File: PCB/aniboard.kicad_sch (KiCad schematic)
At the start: 416 parts, among them J2 Conn_01x02_Pin, J3 Conn_01x02_Pin, J5 Conn_01x03_Pin, J6 USB_C_Receptacle_USB2.0_14P, J7 USB_C_Receptacle_USB2.0_14P, SW1 SW_Push, SW10 SW_Push, SW11 SW_Push, SW12 SW_Push, SW13 SW_Push, SW14 SW_Push, SW15 SW_Push, SW16 SW_Push, SW17 SW_Push, SW18 SW_Push, SW19 SW_Push, SW2 SW_Push, SW20 SW_Push, SW21 SW_Push, SW22 SW_Push, SW23 SW_Push, SW24 SW_Push, SW25 SW_Push, SW26 SW_Push, SW27 SW_Push, SW28 SW_Push, SW29 SW_Push, SW3 SW_Push, SW30 SW_Push, SW31 SW_Push, SW32 SW_Push, SW33 SW_Push, SW34 SW_Push, SW35 SW_Push, SW36 SW_Push, SW37 SW_Push, SW38 SW_Push, SW39 SW_Push, SW4 SW_Push, SW40 SW_Push, SW41 SW_Push, SW42 SW_Push, SW43 SW_Push, SW44 SW_Push, SW45 SW_Push, SW46 SW_Push, SW47 SW_Push, SW48 SW_Push, SW49 SW_Push, SW5 SW_Push, SW50 SW_Push, SW51 SW_Push, SW52 SW_Push, SW53 SW_Push, SW54 SW_Push, SW55 SW_Push, SW56 SW_Push, SW57 SW_Push, SW58 SW_Push, SW59 SW_Push, SW6 SW_Push, SW60 SW_Push, SW61 SW_Push, SW62 SW_Push, SW63 SW_Push, SW64 SW_Push, SW65 SW_Push, SW66 SW_Push, SW67 SW_Push, SW68 SW_Push, SW69 SW_Push, SW7 SW_Push, SW70 SW_Push, SW71 SW_Push, SW72 SW_Push, SW73 SW_Push, SW74 SW_Push, SW75 SW_Push, SW76 SW_Push, SW77 SW_Push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

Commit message: V4
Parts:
- added D95: LED, LED_SMD:LED_0603_1608Metric_Pad1.05x0.95mm_HandSolder, symbol Device:LED
- added R20: 200Ω, Resistor_SMD:R_0805_2012Metric_Pad1.20x1.40mm_HandSolder, symbol Device:R
- added U7: ESP-12E, RF_Module:ESP-12E, symbol RF_Module:ESP-12E
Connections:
- net +3.3V: now also U7.1 (~{RST}), U7.3 (EN), U7.8 (VCC)
- net GND: now also R20.1, U7.15 (GND)
- net SCL: now reaches Brd1.3 (SCL), R10.2, U4.7 (GPIO5)
- net SCL: now also U7.5 (GPIO14)
- net SDA: now reaches Brd1.4 (SDA), R11.2, U4.6 (GPIO4)
- net SDA: now also U7.17 (GPIO2)
- new net: D95.2 (A), U7.7 (GPIO13)
- new net: D95.1 (K), R20.2
- no-connect marks 5 -> 20
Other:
- note added: "Bluetooth module"

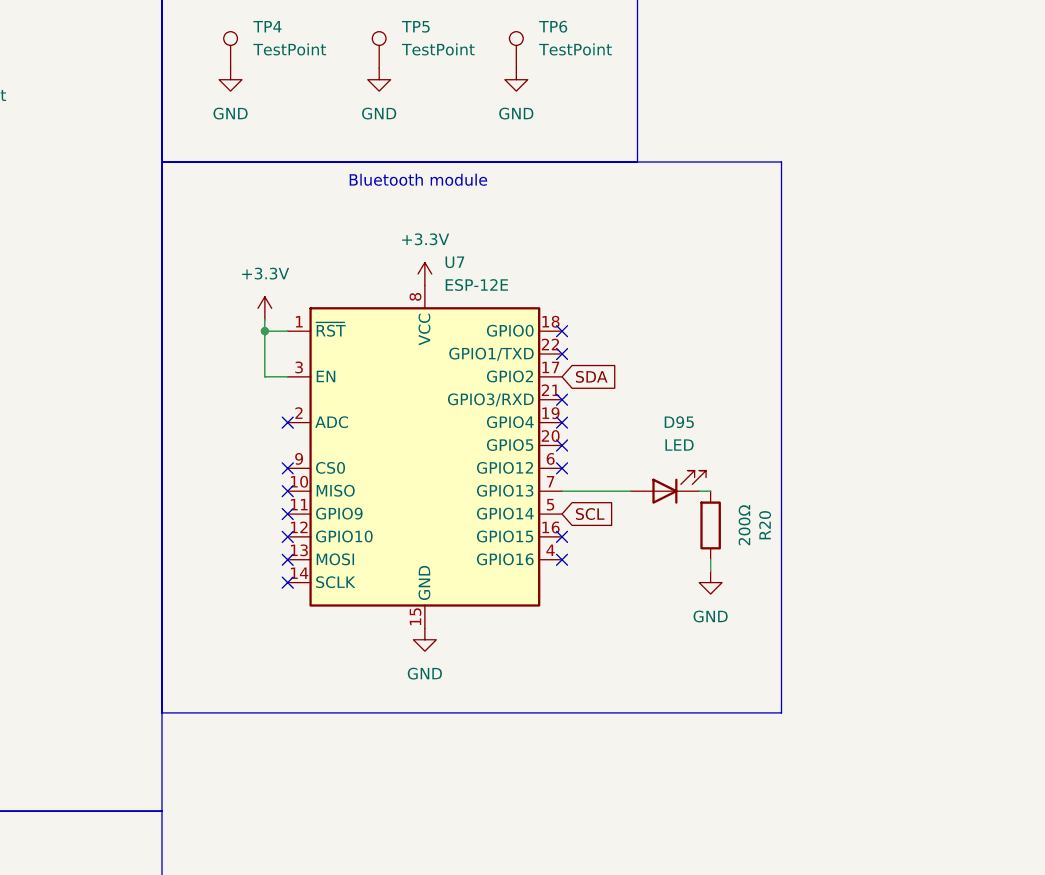
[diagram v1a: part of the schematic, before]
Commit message: RX TX Breakout
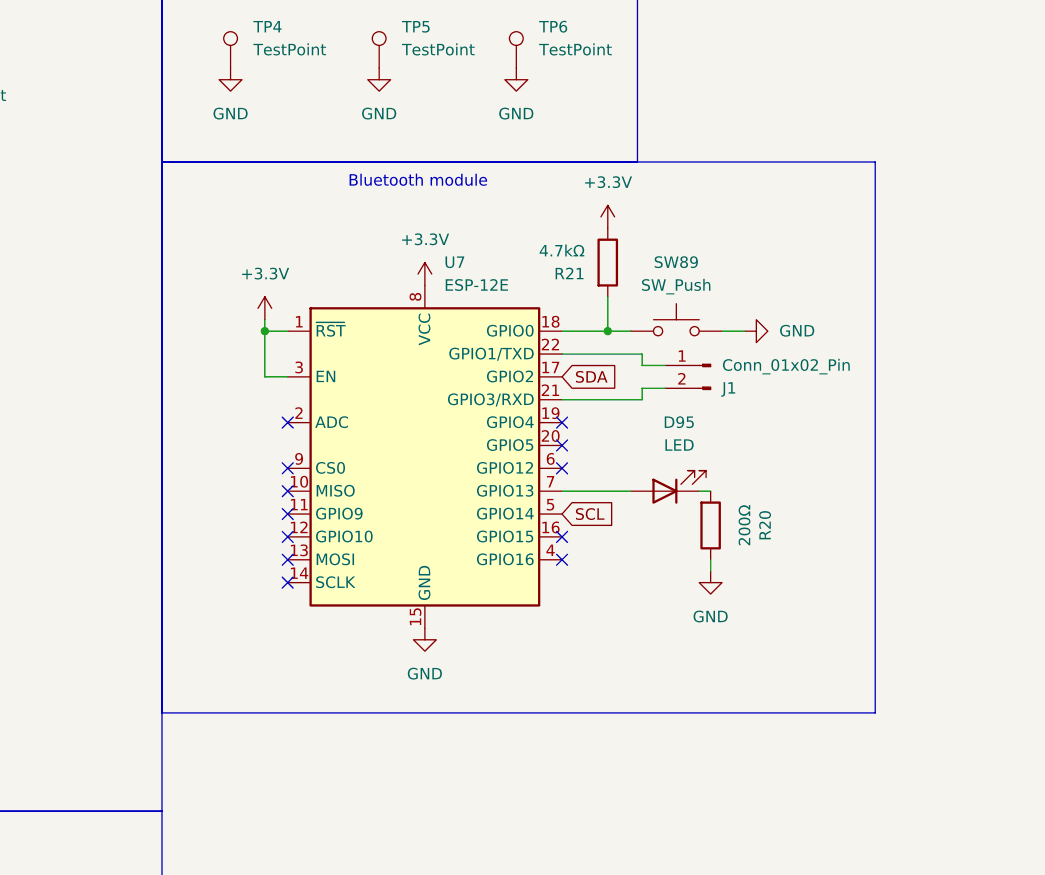
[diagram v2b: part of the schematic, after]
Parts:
- added J1: Conn_01x02_Pin, Connector_PinSocket_2.54mm:PinSocket_1x02_P2.54mm_Vertical, symbol Connector:Conn_01x02_Pin
- added R21: 4.7kΩ, Resistor_SMD:R_0805_2012Metric_Pad1.20x1.40mm_HandSolder, symbol Device:R
- added SW89: SW_Push, Button_Switch_THT:SW_PUSH_6mm, symbol Switch:SW_Push
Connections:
- net +3.3V: now also R21.1
- net GND: now also SW89.2
- net at U7.18 (GPIO0): now also R21.2, SW89.1
- net at U7.21 (GPIO3/RXD): now also J1.2 (Pin_2)
- net at U7.22 (GPIO1/TXD): now also J1.1 (Pin_1)
- no-connect marks 20 -> 17

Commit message: Finally ordered
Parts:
- removed C15, C16, C17: 4.7uf, Capacitor_SMD:C_0805_2012Metric_Pad1.18x1.45mm_HandSolder, symbol Device:C_Polarized
- removed C53: 1uf, Capacitor_SMD:C_0805_2012Metric_Pad1.18x1.45mm_HandSolder, symbol Device:C
- removed D15, D66, D94: LED, LED_SMD:LED_0603_1608Metric_Pad1.05x0.95mm_HandSolder, symbol Device:LED
- removed J2, J3: Conn_01x02_Pin, Connector_PinHeader_2.54mm:PinHeader_1x02_P2.54mm_Vertical, symbol Connector:Conn_01x02_Pin
- removed J7: USB_C_Receptacle_USB2.0_14P, Connector_USB:USB_C_Receptacle_GCT_USB4105-xx-A_16P_TopMnt_Horizontal, symbol Connector:USB_C_Receptacle_USB2.0_14P
- removed JP2, JP8: SolderJumper_2_Open, Jumper:SolderJumper-2_P1.3mm_Open_RoundedPad1.0x1.5mm, symbol Jumper:SolderJumper_2_Open
- removed JP4, JP5, JP6, JP7: SolderJumper_2_Bridged, Jumper:SolderJumper-2_P1.3mm_Bridged_RoundedPad1.0x1.5mm, symbol Jumper:SolderJumper_2_Bridged
- removed R1, R8: 470Ω, Resistor_SMD:R_0805_2012Metric_Pad1.20x1.40mm_HandSolder, symbol Device:R
- removed R17: 10kΩ, Resistor_SMD:R_0805_2012Metric_Pad1.20x1.40mm_HandSolder, symbol Device:R
- removed R18: 1kΩ, Resistor_SMD:R_0805_2012Metric_Pad1.20x1.40mm_HandSolder, symbol Device:R
- removed R19: 200Ω, Resistor_SMD:R_0805_2012Metric_Pad1.20x1.40mm_HandSolder, symbol Device:R
- removed R2, R7: 4.7kΩ, Resistor_SMD:R_0805_2012Metric_Pad1.20x1.40mm_HandSolder, symbol Device:R
- removed R3, R4, R5, R6: 5.1kΩ, Resistor_SMD:R_0805_2012Metric_Pad1.20x1.40mm_HandSolder, symbol Device:R
- removed SW89: SW_Push, Button_Switch_THT:SW_PUSH_6mm, symbol Switch:SW_Push
- removed TP3: TestPoint, TestPoint:TestPoint_Pad_D3.0mm, symbol Connector:TestPoint
- removed U1, U2: TPS2116DRL, Package_TO_SOT_SMD:SOT-583-8, symbol Power_Management:TPS2116DRL
- removed U6: CH224K, Package_SO:SSOP-10-1EP_3.9x4.9mm_P1mm_EP2.1x3.3mm, symbol Interface_USB:CH224K
- C1, C10, C11, C12, C13, C14, C19, C2, C20, C21, C22, C23, C24, C25, C26, C27, C28, C29, C3, C30, C31, C32, C33, C34, C35, C36, C37, C38, C39, C4, C40, C41, C42, C43, C44, C45, C46, C47, C48, C49, C5, C50, C51, C52, C54, C55, C56, C57, C58, C59, C6, C60, C61, C62, C63, C64, C65, C66, C67, C68, C69, C7, C70, C71, C72, C73, C74, C75, C76, C77, C78, C79, C8, C80, C81, C82, C83, C84, C85, C86, C87, C88, C89, C9, C90, C91, C92, C93, C95, C96: LCSC Part # (none) -> C49678
- C18, C94: LCSC Part # (none) -> C28323
- D1, D10, D11, D12, D13, D14, D16, D17, D18, D19, D2, D20, D21, D22, D23, D24, D25, D26, D27, D28, D29, D3, D30, D31, D32, D33, D34, D35, D36, D37, D38, D39, D4, D40, D41, D42, D43, D44, D45, D46, D47, D48, D49, D5, D50, D51, D52, D53, D54, D55, D56, D57, D58, D59, D6, D60, D61, D62, D63, D64, D65, D67, D68, D69, D7, D70, D71, D72, D73, D74, D75, D76, D77, D78, D79, D8, D80, D81, D82, D83, D84, D85, D86, D87, D88, D89, D9, D90: LCSC Part # (none) -> C435829
- D91, D92, D93, D95: LCSC Part # (none) -> C19273151
- J6: footprint Connector_USB:USB_C_Receptacle_GCT_USB4105-xx-A_16P_TopMnt_Horizontal -> Connector_USB:USB_C_Receptacle_HRO_TYPE-C-31-M-12; LCSC Part # (none) -> C2765186
- LED1, LED10, LED11, LED12, LED13, LED14, LED15, LED16, LED17, LED18, LED19, LED2, LED20, LED21, LED22, LED23, LED24, LED25, LED26, LED27, LED28, LED29, LED3, LED30, LED31, LED32, LED33, LED34, LED35, LED36, LED37, LED38, LED39, LED4, LED40, LED41, LED42, LED43, LED44, LED45, LED46, LED47, LED48, LED49, LED5, LED50, LED51, LED52, LED53, LED54, LED55, LED56, LED57, LED58, LED59, LED6, LED60, LED61, LED62, LED63, LED64, LED65, LED66, LED67, LED68, LED69, LED7, LED70, LED71, LED72, LED73, LED74, LED75, LED76, LED77, LED78, LED79, LED8, LED80, LED81, LED82, LED83, LED84, LED85, LED86, LED87, LED88, LED9: value MX_SK6812MINI-E -> SK6812MINI-E; LCSC Part # (none) -> C5149201
- R10, R11, R21: LCSC Part # (none) -> C17673
- R12, R13, R9: LCSC Part # (none) -> C17710
- R14: LCSC Part # (none) -> C17414
- R15: LCSC Part # (none) -> C17513
- R16, R20: LCSC Part # (none) -> C17540
- U3: LCSC Part # (none) -> C7843
- U7: LCSC Part # (none) -> C89297
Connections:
- net +5V: now also C1.1, C10.1, C11.1, C12.1, C13.1, C18.1, C19.1, C2.1, C20.1, C21.1, C22.1, C23.1, C24.1, C25.1, C26.1, C27.1, C28.1, C29.1, C3.1, C30.1, C31.1, C36.1, C37.1, C38.1, C39.1, C4.1, C40.1, C41.1, C42.1, C43.1, C44.1, C45.1, C46.1, C47.1, C48.1, C5.1, C54.1, C55.1, C56.1, C57.1, C58.1, C59.1, C6.1, C60.1, C61.1, C62.1, C63.1, C64.1, C65.1, C7.1, C70.1, C71.1, C72.1, C73.1, C74.1, C75.1, C76.1, C77.1, C78.1, C79.1, C8.1, C80.1, C81.1, C83.1, C84.1, C85.1, C86.1, C87.1, C88.1, C89.1, C9.1, J6.A4 (VBUS), J6.A9 (VBUS), J6.B4 (VBUS), J6.B9 (VBUS), LED1.1 (VDD), LED10.1 (VDD), LED11.1 (VDD), LED12.1 (VDD), LED13.1 (VDD), LED15.1 (VDD), LED16.1 (VDD), LED17.1 (VDD), LED18.1 (VDD), LED19.1 (VDD), LED2.1 (VDD), LED20.1 (VDD), LED21.1 (VDD), LED22.1 (VDD), LED23.1 (VDD), LED24.1 (VDD), LED25.1 (VDD), LED26.1 (VDD), LED27.1 (VDD), LED3.1 (VDD), LED32.1 (VDD), LED33.1 (VDD), LED34.1 (VDD), LED35.1 (VDD), LED36.1 (VDD), LED37.1 (VDD), LED38.1 (VDD), LED39.1 (VDD), LED4.1 (VDD), LED40.1 (VDD), LED41.1 (VDD), LED42.1 (VDD), LED43.1 (VDD), LED44.1 (VDD), LED49.1 (VDD), LED5.1 (VDD), LED50.1 (VDD), LED51.1 (VDD), LED52.1 (VDD), LED53.1 (VDD), LED54.1 (VDD), LED55.1 (VDD), LED56.1 (VDD), LED57.1 (VDD), LED58.1 (VDD), LED59.1 (VDD), LED6.1 (VDD), LED60.1 (VDD), LED65.1 (VDD), LED66.1 (VDD), LED67.1 (VDD), LED68.1 (VDD), LED69.1 (VDD), LED7.1 (VDD), LED70.1 (VDD), LED71.1 (VDD), LED72.1 (VDD), LED73.1 (VDD), LED74.1 (VDD), LED75.1 (VDD), LED76.1 (VDD), LED78.1 (VDD), LED79.1 (VDD), LED8.1 (VDD), LED80.1 (VDD), LED81.1 (VDD), LED82.1 (VDD), LED83.1 (VDD), LED84.1 (VDD), LED9.1 (VDD), R14.1, R15.2, R16.1, TP2.1, U5.9 (CFG1); no longer JP1.2 (B)
- net +5VA: no longer C1.1, C19.1, C2.1, C20.1, C21.1, C22.1, C23.1, C24.1, C3.1, C36.1, C37.1, C38.1, C39.1, C4.1, C40.1, C41.1, C42.1, C5.1, C54.1, C55.1, C56.1, C57.1, C58.1, C59.1, C6.1, C70.1, C71.1, C72.1, C73.1, C74.1, C75.1, C76.1, C83.1, C84.1, C85.1, C86.1, JP1.1 (A), LED1.1 (VDD), LED15.1 (VDD), LED16.1 (VDD), LED17.1 (VDD), LED18.1 (VDD), LED19.1 (VDD), LED2.1 (VDD), LED20.1 (VDD), LED3.1 (VDD), LED32.1 (VDD), LED33.1 (VDD), LED34.1 (VDD), LED35.1 (VDD), LED36.1 (VDD), LED37.1 (VDD), LED38.1 (VDD), LED4.1 (VDD), LED49.1 (VDD), LED5.1 (VDD), LED50.1 (VDD), LED51.1 (VDD), LED52.1 (VDD), LED53.1 (VDD), LED54.1 (VDD), LED6.1 (VDD), LED65.1 (VDD), LED66.1 (VDD), LED67.1 (VDD), LED68.1 (VDD), LED69.1 (VDD), LED70.1 (VDD), LED71.1 (VDD), LED78.1 (VDD), LED79.1 (VDD), LED80.1 (VDD), LED81.1 (VDD), TP2.1
- net +5VB: no longer C10.1, C11.1, C12.1, C13.1, C25.1, C26.1, C27.1, C28.1, C29.1, C30.1, C31.1, C43.1, C44.1, C45.1, C46.1, C47.1, C48.1, C60.1, C61.1, C62.1, C63.1, C64.1, C65.1, C7.1, C77.1, C78.1, C79.1, C8.1, C80.1, C81.1, C87.1, C88.1, C89.1, C9.1, LED10.1 (VDD), LED11.1 (VDD), LED12.1 (VDD), LED13.1 (VDD), LED21.1 (VDD), LED22.1 (VDD), LED23.1 (VDD), LED24.1 (VDD), LED25.1 (VDD), LED26.1 (VDD), LED27.1 (VDD), LED39.1 (VDD), LED40.1 (VDD), LED41.1 (VDD), LED42.1 (VDD), LED43.1 (VDD), LED44.1 (VDD), LED55.1 (VDD), LED56.1 (VDD), LED57.1 (VDD), LED58.1 (VDD), LED59.1 (VDD), LED60.1 (VDD), LED7.1 (VDD), LED72.1 (VDD), LED73.1 (VDD), LED74.1 (VDD), LED75.1 (VDD), LED76.1 (VDD), LED8.1 (VDD), LED82.1 (VDD), LED83.1 (VDD), LED84.1 (VDD), LED9.1 (VDD)
- net GND: now also JP1.2 (B)
- net at R21.2, U7.18 (GPIO0): now also JP1.1 (A)
- net at U5.1 (VDD): now also R15.1; no longer R15.2
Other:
- moved on the sheet: C18, D93, R14, R15, R16, TP2, U5

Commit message: Add ibom
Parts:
- removed D95: LED, LED_SMD:LED_0603_1608Metric_Pad1.05x0.95mm_HandSolder, symbol Device:LED
- added U1: AMS1117-3.3, Package_TO_SOT_SMD:SOT-223-3_TabPin2, symbol Regulator_Linear:AMS1117-3.3
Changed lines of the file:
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@@
 	)
 	(symbol
-		(lib_id "Device:LED")
-		(at 534.67 217.17 180)
-		(unit 1)
-		(exclude_from_sim no)
-		(in_bom yes)
-		(on_board yes)
-		(dnp no)
-		(fields_autoplaced yes)
-		(property "Reference" "D95"
-			(at 536.2575 209.55 0)
-			(effects
-				(font
-					(size 1.27 1.27)
-				)
-			)
-		)
-		(property "Value" "LED"
-			(at 536.2575 212.09 0)
-			(effects
-				(font
-					(size 1.27 1.27)
-				)
-			)
-		)
-		(property "Footprint" "LED_SMD:LED_0603_1608Metric_Pad1.05x0.95mm_HandSolder"
-			(at 534.67 217.17 0)
-			(effects
-				(font
-					(size 1.27 1.27)
-				)
-				(hide yes)
-			)
-		)
-		(property "Datasheet" "~"
-			(at 534.67 217.17 0)
-			(effects
-				(font
-					(size 1.27 1.27)
-				)
-				(hide yes)
-			)
-		)
-		(property "Description" "Light emitting diode"
-			(at 534.67 217.17 0)
-			(effects
-				(font
-					(size 1.27 1.27)
-				)
-				(hide yes)
-			)
-		)
-		(property "LCSC Part #" "C19273151"
-			(at 534.67 217.17 0)
-			(effects
-				(font
-					(size 1.27 1.27)
-				)
-				(hide yes)
-			)
-		)
-		(pin "1"
-		)
-		(pin "2"
-		)
-		(instances
-			(project "aniboard"
-				(path "/6f5b1aad-42fe-4f04-a72c-874b46a1a48f"
-					(reference "D95")
-					(unit 1)
-				)
-			)
-		)
-	)
-	(symbol
 		(lib_id "Switch:SW_Push")
 		(at 34.29 95.25 0)
@@
 					(unit 1)
 				)
+			)
+		)
+	)
+	(symbol
+		(lib_id "Regulator_Linear:AMS1117-3.3")
+		(at 679.45 166.37 0)
+		(unit 1)
+		(exclude_from_sim no)
+		(in_bom yes)
+		(on_board yes)
+		(dnp no)
+		(fields_autoplaced yes)
+		(property "Reference" "U1"
+			(at 679.45 160.02 0)
+			(effects
+				(font
+					(size 1.27 1.27)
+				)
+			)
+		)
+		(property "Value" "AMS1117-3.3"
+			(at 679.45 162.56 0)
+			(effects
+				(font
+					(size 1.27 1.27)
+				)
+			)
+		)
+		(property "Footprint" "Package_TO_SOT_SMD:SOT-223-3_TabPin2"
+			(at 679.45 161.29 0)
+			(effects
+				(font
+					(size 1.27 1.27)
+				)
+				(hide yes)
+			)
+		)
+		(property "Datasheet" "http://www.advanced-monolithic.com/pdf/ds1117.pdf"
+			(at 681.99 172.72 0)
+			(effects
+				(font
+					(size 1.27 1.27)
+				)
+				(hide yes)
+			)
+		)
+		(property "Description" "1A Low Dropout regulator, positive, 3.3V fixed output, SOT-223"
+			(at 679.45 166.37 0)
+			(effects
+				(font
+					(size 1.27 1.27)
+				)
+				(hide yes)
+			)
+		)
+		(pin "2"
+		)
+		(pin "1"
+		)
+		(pin "3"
+		)
+		(instances
+			(project ""
+				(path "/6f5b1aad-42fe-4f04-a72c-874b46a1a48f"
+					(reference "U1")
+					(unit 1)
+				)
